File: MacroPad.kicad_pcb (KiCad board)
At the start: 2 copper layers, 41 parts, among them J1 USB_C_Receptacle, SW1 SW_Push, U1 ATmega32U4-A, Y1 16MHz

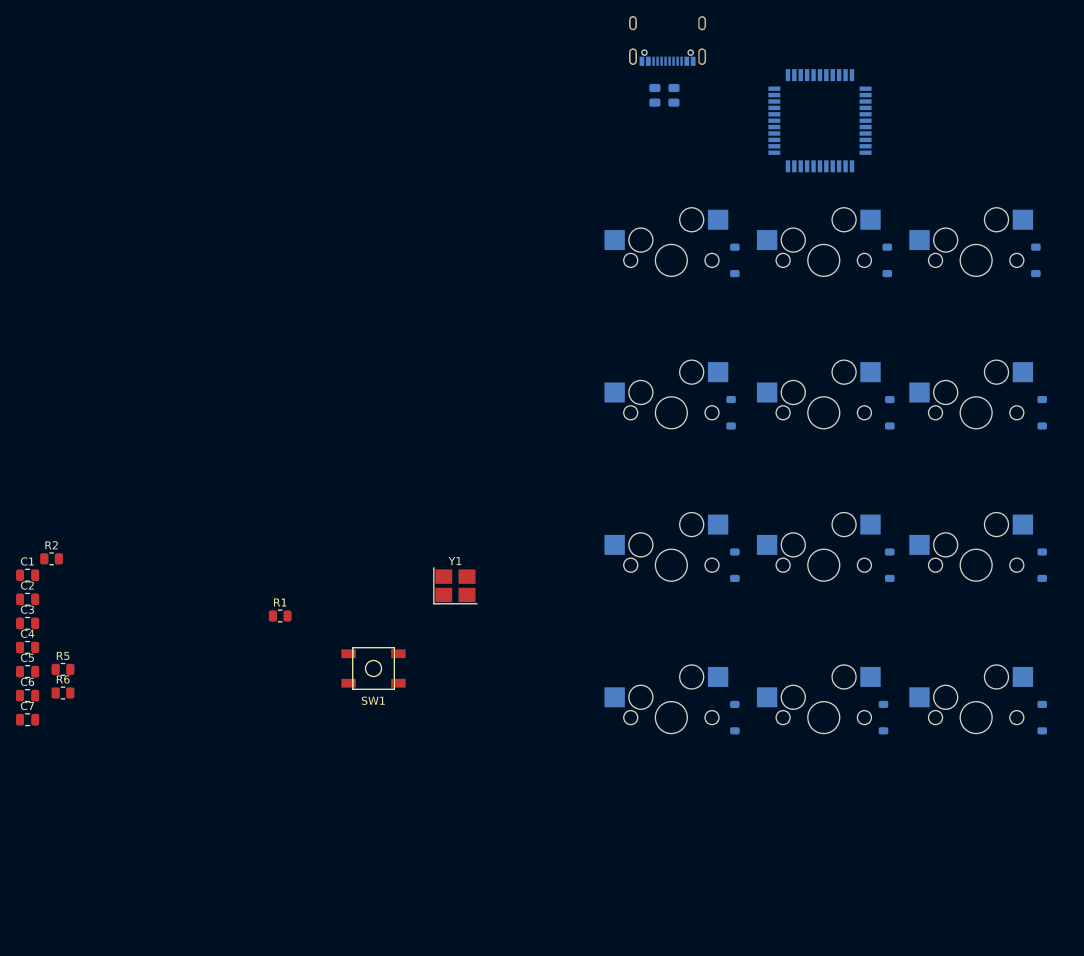
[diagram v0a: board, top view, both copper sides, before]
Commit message: reworked schematic, added footprint library for USB-C, improved component placement
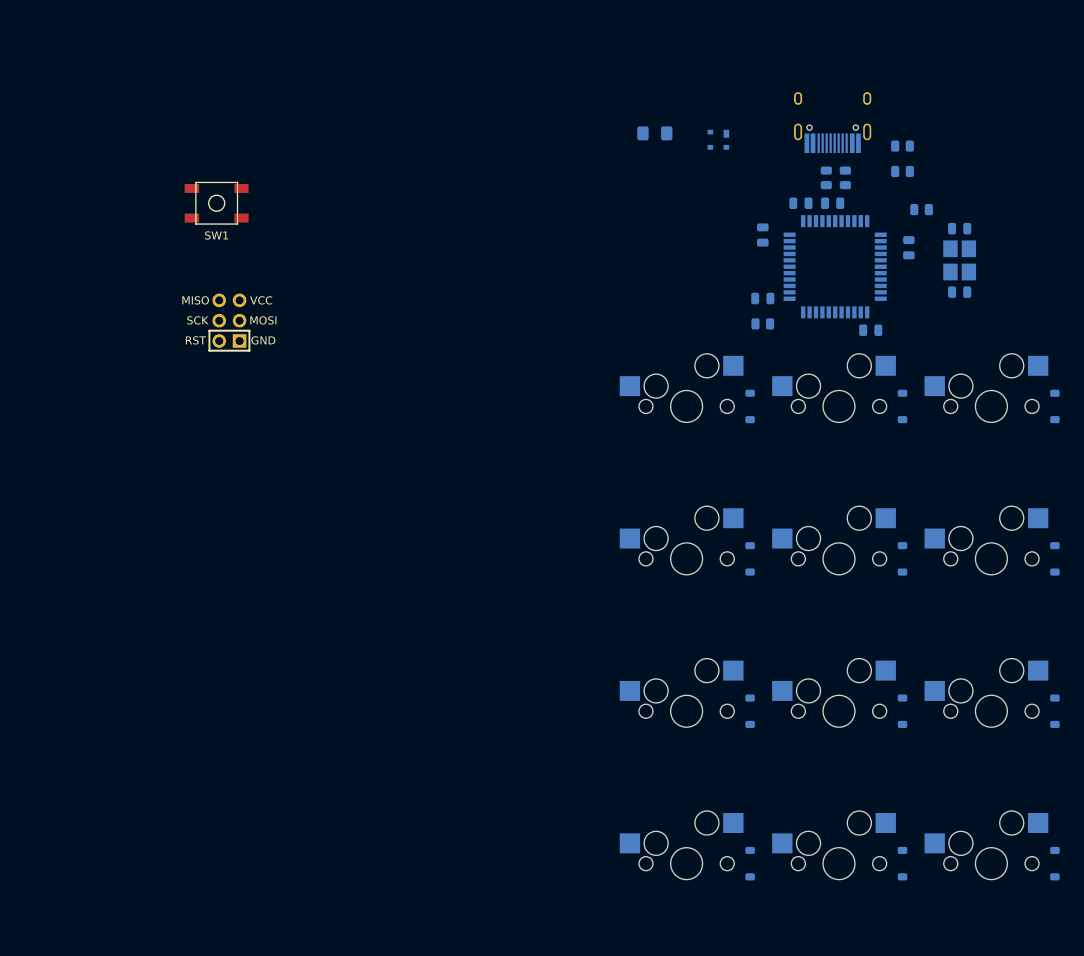
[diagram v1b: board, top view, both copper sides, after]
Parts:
- removed J1: USB_C_Receptacle, Connector_USB:USB_C_Receptacle_GCT_USB4105-xx-A_16P_TopMnt_Horizontal
- added C8: 10u, Capacitor_SMD:C_0805_2012Metric, B.Cu at (154.8, 53.2)
- added D13: PRTR5V0U2X, Package_TO_SOT_SMD:SOT-143, B.Cu at (149.2, 41.3)
- added F1: Polyfuse_Small, Fuse:Fuse_1206_3216Metric_Pad1.42x1.75mm_HandSolder, B.Cu at (141.3, 40.5)
- added J2: AVR-ISP-6, random-keyboard-parts:Reset_Pretty-Mask, F.Cu at (88.1, 63.9)
- added USB1: HRO-TYPE-C-31-M-12, Type-C:HRO-TYPE-C-31-M-12-HandSoldering, B.Cu at (163.5, 33.5)
- C1, C2, C3, C4, C5, C6, R1, R2, R5, R6, Y1: moved to B.Cu
- C7: value 10u -> 0.1u; moved to B.Cu
- moved R6 125.2 mm to (172.2, 42.1), turned to 180 degrees
- moved C1 124.3 mm to (179.4, 52.4)
- moved C2 122.7 mm to (179.4, 60.3), turned to 180 degrees
- moved C4 121.0 mm to (173.0, 54.8), turned to -90 degrees
- moved R2 116.9 mm to (172.2, 45.2), turned to 180 degrees
- moved C6 114.6 mm to (159.5, 49.2), turned to 180 degrees
- moved C5 113.7 mm to (168.3, 65.1)
- moved C3 113.5 mm to (163.5, 49.2), turned to 180 degrees
- moved C7 105.9 mm to (154.8, 61.1), turned to 180 degrees
- moved R5 97.6 mm to (154.8, 64.3), turned to 180 degrees
- moved R1 94.9 mm to (174.6, 50.0), turned to 180 degrees
- moved Y1 75.0 mm to (179.4, 56.4), turned to -90 degrees
- moved SW1 61.4 mm to (86.5, 49.2)
- moved R3 26.0 mm to (165.1, 46.0)
- moved R4 21.7 mm to (162.7, 46.0)
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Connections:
- net Net-(U1-~{RESET}) renamed RESET
- U1 pad 10: unconnected-(U1-PB2-Pad10) -> MOSI
- U1 pad 11: unconnected-(U1-PB3-Pad11) -> SCK
- U1 pad 18: ROW0 -> unconnected-(U1-PD0-Pad18)
- U1 pad 19: ROW1 -> unconnected-(U1-PD1-Pad19)
- U1 pad 20: ROW2 -> unconnected-(U1-PD2-Pad20)
- U1 pad 21: ROW3 -> unconnected-(U1-PD3-Pad21)
- U1 pad 26: unconnected-(U1-PD6-Pad26) -> ROW0
- U1 pad 27: unconnected-(U1-PD7-Pad27) -> ROW1
- U1 pad 28: COL0 -> ROW2
- U1 pad 29: COL1 -> ROW3
- U1 pad 31: unconnected-(U1-PC6-Pad31) -> COL1
- U1 pad 32: unconnected-(U1-PC7-Pad32) -> COL0
- U1 pad 9: unconnected-(U1-PB1-Pad9) -> MISO

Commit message: finished placement, routing and overall layout
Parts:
- added REF**: MountingHole_2.7mm_M2.5, MountingHole:MountingHole_2.7mm_M2.5, F.Cu at (154.8, 122.2)
- added REF**: MountingHole_2.7mm_M2.5, MountingHole:MountingHole_2.7mm_M2.5, F.Cu at (173.8, 122.2)
- added REF**: MountingHole_2.7mm_M2.5, MountingHole:MountingHole_2.7mm_M2.5, F.Cu at (173.8, 65.1)
- added REF**: MountingHole_2.7mm_M2.5, MountingHole:MountingHole_2.7mm_M2.5, F.Cu at (154.8, 65.1)
- J2, SW1: moved to B.Cu
- moved SW1 61.0 mm to (147.5, 49.8), turned to 180 degrees
- moved J2 59.4 mm to (147.3, 58.4), turned to 180 degrees
- moved R5 36.2 mm to (190.7, 59.5), turned to -90 degrees
- moved C7 32.2 mm to (186.9, 62.0), turned to -90 degrees
- moved C5 28.4 mm to (190.7, 47.8), turned to 90 degrees
- moved C8 25.4 mm to (178.6, 62.2)
- moved F1 23.0 mm to (160.3, 53.4), turned to 90 degrees
- moved U1 19.1 mm to (182.6, 53.2), turned to 0 degrees
- moved C2 17.7 mm to (179.9, 42.6), turned to -90 degrees
- moved D13 17.4 mm to (164.3, 50.0)
- moved C6 16.6 mm to (172.8, 59.2)
- moved Y1 14.4 mm to (183.8, 42.6), turned to 180 degrees
- moved R6 13.7 mm to (160.3, 48.8), turned to 0 degrees
- moved C1 13.4 mm to (187.8, 42.0), turned to -90 degrees
- moved C4 12.9 mm to (177.5, 42.7), turned to 90 degrees
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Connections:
- net Net-(U1-D+) renamed DP
- net Net-(U1-D-) renamed DN
- U1 pad 1: unconnected-(U1-PE6-Pad1) -> COL0
- U1 pad 26: ROW0 -> unconnected-(U1-PD6-Pad26)
- U1 pad 27: ROW1 -> unconnected-(U1-PD7-Pad27)
- U1 pad 28: ROW2 -> unconnected-(U1-PB4-Pad28)
- U1 pad 29: ROW3 -> unconnected-(U1-PB5-Pad29)
- U1 pad 30: COL2 -> unconnected-(U1-PB6-Pad30)
- U1 pad 31: COL1 -> unconnected-(U1-PC6-Pad31)
- U1 pad 32: COL0 -> unconnected-(U1-PC7-Pad32)
- U1 pad 36: unconnected-(U1-PF7-Pad36) -> ROW0
- U1 pad 37: unconnected-(U1-PF6-Pad37) -> ROW1
- U1 pad 38: unconnected-(U1-PF5-Pad38) -> ROW2
- U1 pad 39: unconnected-(U1-PF4-Pad39) -> ROW3
- U1 pad 40: unconnected-(U1-PF1-Pad40) -> COL2
- U1 pad 41: unconnected-(U1-PF0-Pad41) -> COL1
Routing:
- net +5V: track 0.00 -> 133.1 mm, vias 0 -> 6
- net ROW3: track 0.00 -> 130.0 mm
- net ROW2: track 0.00 -> 109.2 mm, vias 0 -> 3
- net COL0: track 0.00 -> 104.2 mm
- net COL1: track 0.00 -> 91.1 mm
- net ROW1: track 0.00 -> 87.1 mm, vias 0 -> 3
- net COL2: track 0.00 -> 72.6 mm
- net ROW0: track 0.00 -> 66.7 mm, vias 0 -> 3
- net RESET: track 0.00 -> 62.0 mm, vias 0 -> 1
- net GND: track 0.00 -> 48.3 mm, vias 0 -> 65
- net MOSI: track 0.00 -> 40.1 mm, vias 0 -> 1
- net SCK: track 0.00 -> 36.5 mm, vias 0 -> 1
- net MISO: track 0.00 -> 35.7 mm, vias 0 -> 1
- net VBUS: track 0.00 -> 20.0 mm, vias 0 -> 2
- net D+: track 0.00 -> 19.4 mm
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- added copper zone on B.Cu, net GND
- added copper zone on F.Cu, net GND
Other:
- board outline added: 57.2 x 103.2 mm

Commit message: Added B. Silkscreen notes
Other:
- board text added: "Hamel Electronics Designed by Jeffrey Hamel"
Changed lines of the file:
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@@
     (property "Sheetname" "")
     (attr smd)
-    (fp_text reference "USB1" (at -6.82625 4.712) (layer "B.SilkS")
+    (fp_text reference "USB1" (at 7.14375 4.712) (layer "B.SilkS")
         (effects (font (size 1 1) (thickness 0.153)) (justify mirror))
     )
@@
   (gr_line (start 135.73125 39.6875) (end 135.73125 139.7)
     (stroke (width 0.1) (type default)) (layer "Edge.Cuts"))
+  (gr_text "Hamel Electronics\nDesigned by Jeffrey Hamel" (at 157.988 43.307) (layer "B.SilkS")
+    (effects (font (size 1.2 1) (thickness 0.2)) (justify left bottom mirror))
+  )
   (segment (start 163.957 60.198) (end 163.703 60.198) (width 0.254) (layer "F.Cu") (net 1))
   (segment (start 170.307 62.738) (end 174.498 62.738) (width 0.381) (layer "F.Cu") (net 1))
